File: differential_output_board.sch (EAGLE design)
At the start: 18 parts, among them IC1 ATA6563

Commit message: fixed CAN termination for cat6 wiring
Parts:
- R1, R2, R3, R4: value 62R -> 49R9; MOUSER 652-CR1206FX-62R0ELF -> 71-CRCW120649R9FKEAC
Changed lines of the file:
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@@
 <part name="+3V4" library="supply1" library_urn="urn:adsk.eagle:library:371" deviceset="+3V3" device=""/>
 <part name="GND5" library="supply1" library_urn="urn:adsk.eagle:library:371" deviceset="GND" device=""/>
-<part name="R1" library="rcl" library_urn="urn:adsk.eagle:library:334" deviceset="R-EU_" device="M1206" package3d_urn="urn:adsk.eagle:package:23566/1" value="62R">
+<part name="R1" library="rcl" library_urn="urn:adsk.eagle:library:334" deviceset="R-EU_" device="M1206" package3d_urn="urn:adsk.eagle:package:23566/1" value="49R9">
 <spice>
 <pinmapping spiceprefix="R">
@@
 </pinmapping>
 </spice>
-<attribute name="MOUSER" value="652-CR1206FX-62R0ELF"/>
+<attribute name="MOUSER" value="71-CRCW120649R9FKEAC"/>
 </part>
-<part name="R2" library="rcl" library_urn="urn:adsk.eagle:library:334" deviceset="R-EU_" device="M1206" package3d_urn="urn:adsk.eagle:package:23566/1" value="62R">
+<part name="R2" library="rcl" library_urn="urn:adsk.eagle:library:334" deviceset="R-EU_" device="M1206" package3d_urn="urn:adsk.eagle:package:23566/1" value="49R9">
 <spice>
 <pinmapping spiceprefix="R">
@@
 </pinmapping>
 </spice>
-<attribute name="MOUSER" value="652-CR1206FX-62R0ELF"/>
+<attribute name="MOUSER" value="71-CRCW120649R9FKEAC"/>
 </part>
 <part name="C7" library="rcl" library_urn="urn:adsk.eagle:library:334" deviceset="C-EU" device="C0805" package3d_urn="urn:adsk.eagle:package:23617/2" value="4.7nF">
@@
 </part>
 <part name="GND6" library="supply1" library_urn="urn:adsk.eagle:library:371" deviceset="GND" device=""/>
-<part name="R3" library="rcl" library_urn="urn:adsk.eagle:library:334" deviceset="R-EU_" device="M1206" package3d_urn="urn:adsk.eagle:package:23566/1" value="62R">
+<part name="R3" library="rcl" library_urn="urn:adsk.eagle:library:334" deviceset="R-EU_" device="M1206" package3d_urn="urn:adsk.eagle:package:23566/1" value="49R9">
 <spice>
 <pinmapping spiceprefix="R">
@@
 </pinmapping>
 </spice>
-<attribute name="MOUSER" value="652-CR1206FX-62R0ELF"/>
+<attribute name="MOUSER" value="71-CRCW120649R9FKEAC"/>
 </part>
-<part name="R4" library="rcl" library_urn="urn:adsk.eagle:library:334" deviceset="R-EU_" device="M1206" package3d_urn="urn:adsk.eagle:package:23566/1" value="62R">
+<part name="R4" library="rcl" library_urn="urn:adsk.eagle:library:334" deviceset="R-EU_" device="M1206" package3d_urn="urn:adsk.eagle:package:23566/1" value="49R9">
 <spice>
 <pinmapping spiceprefix="R">
@@
 </pinmapping>
 </spice>
-<attribute name="MOUSER" value="652-CR1206FX-62R0ELF"/>
+<attribute name="MOUSER" value="71-CRCW120649R9FKEAC"/>
 </part>
 <part name="C8" library="rcl" library_urn="urn:adsk.eagle:library:334" deviceset="C-EU" device="C0805" package3d_urn="urn:adsk.eagle:package:23617/2" value="4.7nF">

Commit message: added status LEDs for power on differential output board
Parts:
- added LED1, LED2: (no value), led:LEDCHIPLED_1206
- added R5: 1k2, rcl:R-EU_M0805
- added R6: 680R, rcl:R-EU_M0805
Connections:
- new net N$13: LED1.A, R5.2
- new net N$14: LED2.A, R6.2
- net +3V3: now also R6.1
- net +5V: now also R5.1
- net GND: now also LED1.C, LED2.C
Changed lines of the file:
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@@
 <part name="SV4" library="lichtenstein_onion" deviceset="SS-51000-003" device=""/>
 <part name="SV5" library="lichtenstein_onion" deviceset="SS-51000-003" device=""/>
+<part name="LED1" library="led" library_urn="urn:adsk.eagle:library:259" deviceset="LED" device="CHIPLED_1206" package3d_urn="urn:adsk.eagle:package:15823/2">
+<attribute name="MOUSER" value="604-APTR3216SGC"/>
+</part>
+<part name="LED2" library="led" library_urn="urn:adsk.eagle:library:259" deviceset="LED" device="CHIPLED_1206" package3d_urn="urn:adsk.eagle:package:15823/2">
+<attribute name="MOUSER" value="604-APTR3216SGC"/>
+</part>
+<part name="R5" library="rcl" library_urn="urn:adsk.eagle:library:334" deviceset="R-EU_" device="M0805" package3d_urn="urn:adsk.eagle:package:23556/1" value="1k2">
+<attribute name="MOUSER" value="652-CR0805FX-1201ELF"/>
+</part>
+<part name="R6" library="rcl" library_urn="urn:adsk.eagle:library:334" deviceset="R-EU_" device="M0805" package3d_urn="urn:adsk.eagle:package:23556/1" value="680R">
+<attribute name="MOUSER" value="652-CR0805-FX6800GLF"/>
+</part>
+<part name="GND15" library="supply1" library_urn="urn:adsk.eagle:library:371" deviceset="GND" device=""/>
+<part name="P+5" library="supply1" library_urn="urn:adsk.eagle:library:371" deviceset="+5V" device=""/>
+<part name="+3V5" library="supply1" library_urn="urn:adsk.eagle:library:371" deviceset="+3V3" device=""/>
 </parts>
 <sheets>
@@
 <instance part="SV4" gate="G$1" x="40.64" y="180.34"/>
 <instance part="SV5" gate="G$1" x="40.64" y="152.4"/>
+<instance part="LED1" gate="G$1" x="35.56" y="63.5" rot="R90">
+<attribute name="MOUSER" x="35.56" y="63.5" size="1.27" layer="96" rot="R90" align="top-center" display="off"/>
+</instance>
+<instance part="LED2" gate="G$1" x="35.56" y="55.88" rot="R90">
+<attribute name="MOUSER" x="35.56" y="55.88" size="1.27" layer="96" rot="R90" align="top-center" display="off"/>
+</instance>
+<instance part="R5" gate="G$1" x="27.94" y="63.5">
+<attribute name="MOUSER" x="27.94" y="63.5" size="1.27" layer="96" align="top-center" display="off"/>
+</instance>
+<instance part="R6" gate="G$1" x="27.94" y="55.88">
+<attribute name="MOUSER" x="27.94" y="55.88" size="1.27" layer="96" align="top-center" display="off"/>
+</instance>
+<instance part="GND15" gate="1" x="43.18" y="63.5" smashed="yes" rot="R90">
+<attribute name="VALUE" x="45.72" y="63.5" size="1.778" layer="96"/>
+</instance>
+<instance part="P+5" gate="1" x="20.32" y="63.5" smashed="yes" rot="R90">
+<attribute name="VALUE" x="17.78" y="63.5" size="1.778" layer="96" rot="R180"/>
+</instance>
+<instance part="+3V5" gate="G$1" x="20.32" y="55.88" smashed="yes" rot="R90">
+<attribute name="VALUE" x="17.78" y="55.88" size="1.778" layer="96" rot="R180"/>
+</instance>
 </instances>
 <busses>
@@
 <pinref part="+3V4" gate="G$1" pin="+3V3"/>
 <junction x="187.96" y="78.74"/>
+</segment>
+<segment>
+<pinref part="R6" gate="G$1" pin="1"/>
+<pinref part="+3V5" gate="G$1" pin="+3V3"/>
+<junction x="22.86" y="55.88"/>
 </segment>
 </net>
@@
 <junction x="121.92" y="20.32"/>
 </segment>
+<segment>
+<pinref part="LED2" gate="G$1" pin="C"/>
+<pinref part="LED1" gate="G$1" pin="C"/>
+<wire x1="40.64" y1="63.5" x2="40.64" y2="55.88" width="0.1524" layer="91"/>
+<pinref part="GND15" gate="1" pin="GND"/>
+<junction x="40.64" y="63.5"/>
+</segment>
 </net>
 <net name="OUT3_N" class="0">
@@
 <junction x="198.12" y="78.74"/>
 </segment>
+<segment>
+<pinref part="R5" gate="G$1" pin="1"/>
+<pinref part="P+5" gate="1" pin="+5V"/>
+<junction x="22.86" y="63.5"/>
+</segment>
 </net>
 <net name="CAN_TX" class="0">
@@
 </segment>
 </net>
+<net name="N$13" class="0">
+<segment>
+<pinref part="LED1" gate="G$1" pin="A"/>
+<pinref part="R5" gate="G$1" pin="2"/>
+<junction x="33.02" y="63.5"/>
+</segment>
+</net>
+<net name="N$14" class="0">
+<segment>
+<pinref part="LED2" gate="G$1" pin="A"/>
+<pinref part="R6" gate="G$1" pin="2"/>
+<junction x="33.02" y="55.88"/>
+</segment>
+</net>

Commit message: routed differential output board
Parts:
- added WEED1: WEED, lichtenstein_onion:WEED
- C2: value 10µF -> 100nF; device rcl:CPOL-EUSMCB -> rcl:C-EUC0805; MOUSER 581-TAJB106K020RNJV -> 710-885012207072
- C3: value 100nF -> 47µF; device rcl:C-EUC0805 -> rcl:CPOL-EUCT6032; MOUSER 710-885012207072 -> 581-TAJD476M016RNJV
- C4: value 100nF -> 10µF; device rcl:C-EUC0805 -> rcl:CPOL-EUSMCB; MOUSER 710-885012207072 -> 581-TAJB106K020RNJV
- C5: value 100nF -> 4.7nF; MOUSER 710-885012207072 -> 710-885012207037
- C6: value 47µF -> 4.7nF; device rcl:CPOL-EUCT6032 -> rcl:C-EUC0805; MOUSER 581-TAJD476M016RNJV -> 710-885012207037
- C7, C8: value 4.7nF -> 100nF; MOUSER 710-885012207037 -> 710-885012207072
- R1: value 49R9 -> 1k2; device rcl:R-EU_M1206 -> rcl:R-EU_M0805; MOUSER 71-CRCW120649R9FKEAC -> 652-CR0805FX-1201ELF
- R2: value 49R9 -> 680R; device rcl:R-EU_M1206 -> rcl:R-EU_M0805; MOUSER 71-CRCW120649R9FKEAC -> 652-CR0805-FX6800GLF
- R5: value 1k2 -> 49R9; device rcl:R-EU_M0805 -> rcl:R-EU_M1206; MOUSER 652-CR0805FX-1201ELF -> 71-CRCW120649R9FKEAC
- R6: value 680R -> 49R9; device rcl:R-EU_M0805 -> rcl:R-EU_M1206; MOUSER 652-CR0805-FX6800GLF -> 71-CRCW120649R9FKEAC
- SV2: value (none) -> SS-51000-003; device con-lstb:MA12-2 -> lichtenstein_onion:SS-51000-003; MOUSER 517-30320-6002 -> (none)
- SV3: value SS-51000-003 -> (none); device lichtenstein_onion:SS-51000-003 -> con-lstb:MA12-2; MOUSER (none) -> 517-30320-6002
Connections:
- net +3V3: now also C2.1, C4.+, C7.1, R2.1, SV3.2; no longer C1.1, C2.+, C4.1, R6.1, SV2.2
- net +5V: now also C1.1, C3.+, C8.1, R1.1, SV3.4; no longer C3.1, C5.1, C6.+, R5.1, SV2.4
- net CANH: now also R3.2, SV1.6; no longer R1.2, SV1.5
- net CANH_1: now also SV1.8, SV2.6; no longer SV1.7, SV3.5
- net CANH_2: now also SV2.8, SV4.6; no longer SV3.7, SV4.5
- net CANH_3: now also SV4.8, SV5.6; no longer SV4.7, SV5.5
- net CANH_4: now also R5.1, SV5.8; no longer R4.1, SV5.7
- net CANL: now also R4.1, SV1.5; no longer R2.1, SV1.6
- net CANL_1: now also SV1.7, SV2.5; no longer SV1.8, SV3.6
- net CANL_2: now also SV2.7, SV4.5; no longer SV3.8, SV4.6
- net CANL_3: now also SV4.7, SV5.5; no longer SV4.8, SV5.6
- net CANL_4: now also R6.2, SV5.7; no longer R3.2, SV5.8
- net CAN_RX: now also SV3.23; no longer SV2.23
- net CAN_TX: now also SV3.24; no longer SV2.24
- net GND: now also C2.2, C3.-, C4.-, C6.2, SV3.1, SV3.21, SV3.22, SV3.3; no longer C2.-, C3.2, C4.2, C6.-, SV2.1, SV2.21, SV2.22, SV2.3
- net N$1: now also C5.1, R3.1, R4.2; no longer C7.1, R1.1, R2.2
- net N$13: now also R1.2; no longer R5.2
- net N$14: now also R2.2; no longer R6.2
- net N$2: now also C6.1, R5.2, R6.1; no longer C8.1, R3.1, R4.2
- net OUT0_N: now also SV1.1, SV3.20; no longer SV1.2, SV2.8
- net OUT0_P: now also SV1.2, SV3.18; no longer SV1.1, SV2.6
- net OUT1_N: now also SV1.3, SV3.16; no longer SV1.4, SV2.12
- net OUT1_P: now also SV1.4, SV3.14; no longer SV1.3, SV2.10
- net OUT2_N: now also SV2.1, SV3.12; no longer SV2.16, SV3.2
- net OUT2_P: now also SV2.2, SV3.10; no longer SV2.14, SV3.1
- net OUT3_N: now also SV2.3, SV3.8; no longer SV2.20, SV3.4, SV4.2
- net OUT3_P: now also SV2.4, SV3.6; no longer SV2.18, SV3.3, SV4.1
- net OUT4_N: now also SV3.7, SV4.3; no longer SV2.7, SV4.4
- net OUT4_P: now also SV3.5, SV4.4; no longer SV2.5, SV4.3
- net OUT5_N: now also SV3.11, SV4.1; no longer SV2.11, SV5.2
- net OUT5_P: now also SV3.9, SV4.2; no longer SV2.9, SV5.1
- net OUT6_N: now also SV3.15, SV5.3; no longer SV2.15, SV5.4
- net OUT6_P: now also SV3.13, SV5.4; no longer SV2.13, SV5.3
- net OUT7_N: now also SV3.19, SV5.1; no longer SV2.19
- net OUT7_P: now also SV3.17, SV5.2; no longer SV2.17
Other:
- moved on the sheet: C1, C5, C7, C8, R1, R2, R3, R4, R5, R6

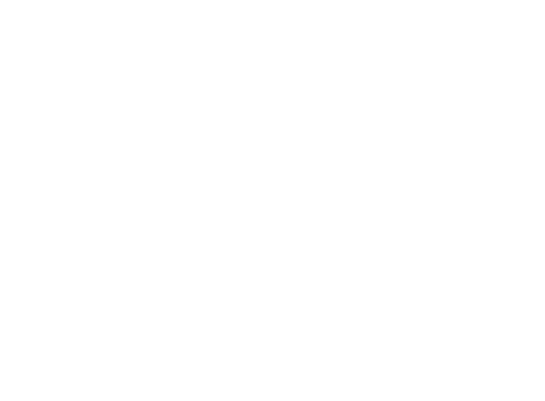
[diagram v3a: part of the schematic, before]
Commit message: added holes to differential output board
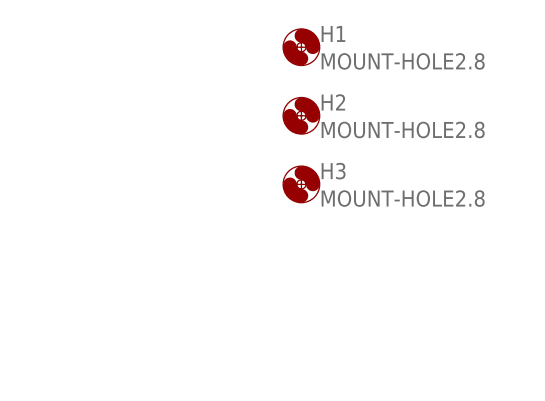
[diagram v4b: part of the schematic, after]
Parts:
- added H1, H2, H3: MOUNT-HOLE2.8, holes:MOUNT-HOLE2.8
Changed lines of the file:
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@@
 <part name="+3V32" library="supply1" library_urn="urn:adsk.eagle:library:371" deviceset="+3V3" device=""/>
 <part name="WEED1" library="lichtenstein_onion" deviceset="WEED" device=""/>
+<part name="H1" library="holes" library_urn="urn:adsk.eagle:library:237" deviceset="MOUNT-HOLE" device="2.8" package3d_urn="urn:adsk.eagle:package:14271/1"/>
+<part name="H2" library="holes" library_urn="urn:adsk.eagle:library:237" deviceset="MOUNT-HOLE" device="2.8" package3d_urn="urn:adsk.eagle:package:14271/1"/>
+<part name="H3" library="holes" library_urn="urn:adsk.eagle:library:237" deviceset="MOUNT-HOLE" device="2.8" package3d_urn="urn:adsk.eagle:package:14271/1"/>
 </parts>
 <sheets>
@@
 </instance>
 <instance part="WEED1" gate="G$1" x="147.32" y="38.1"/>
+<instance part="H1" gate="G$1" x="223.52" y="180.34"/>
+<instance part="H2" gate="G$1" x="223.52" y="172.72"/>
+<instance part="H3" gate="G$1" x="223.52" y="165.1"/>
 </instances>
 <busses>

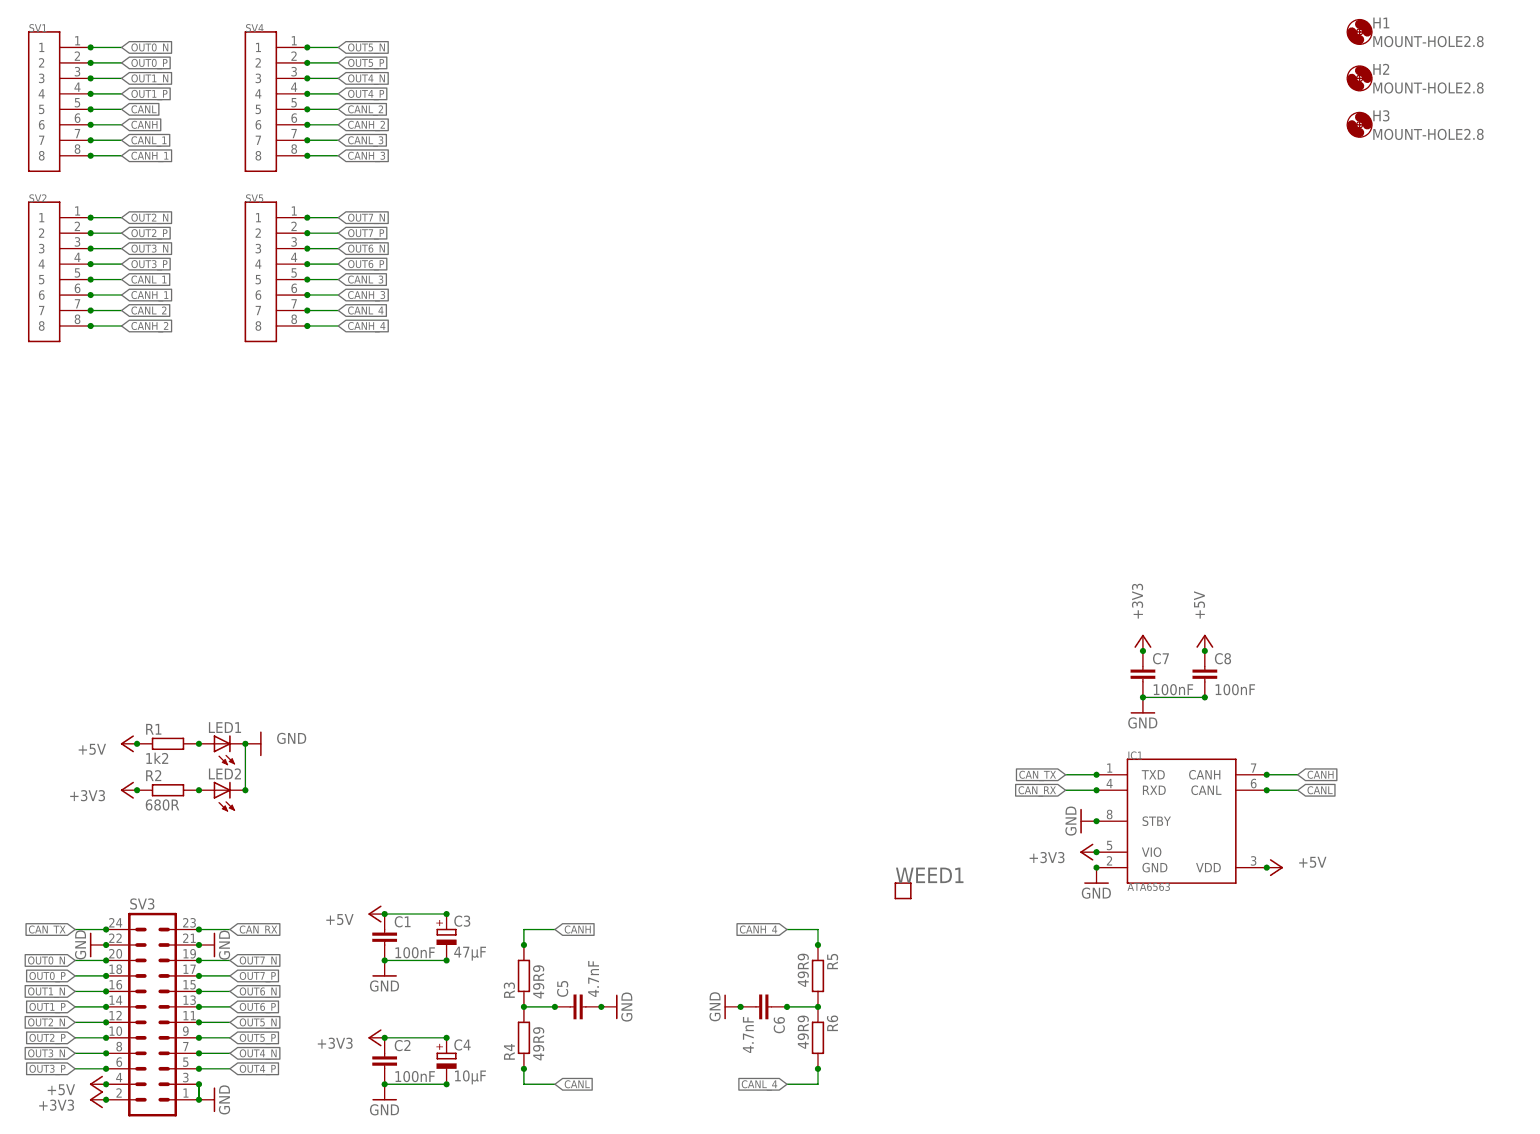
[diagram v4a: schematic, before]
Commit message: More tweaks to the differential output board
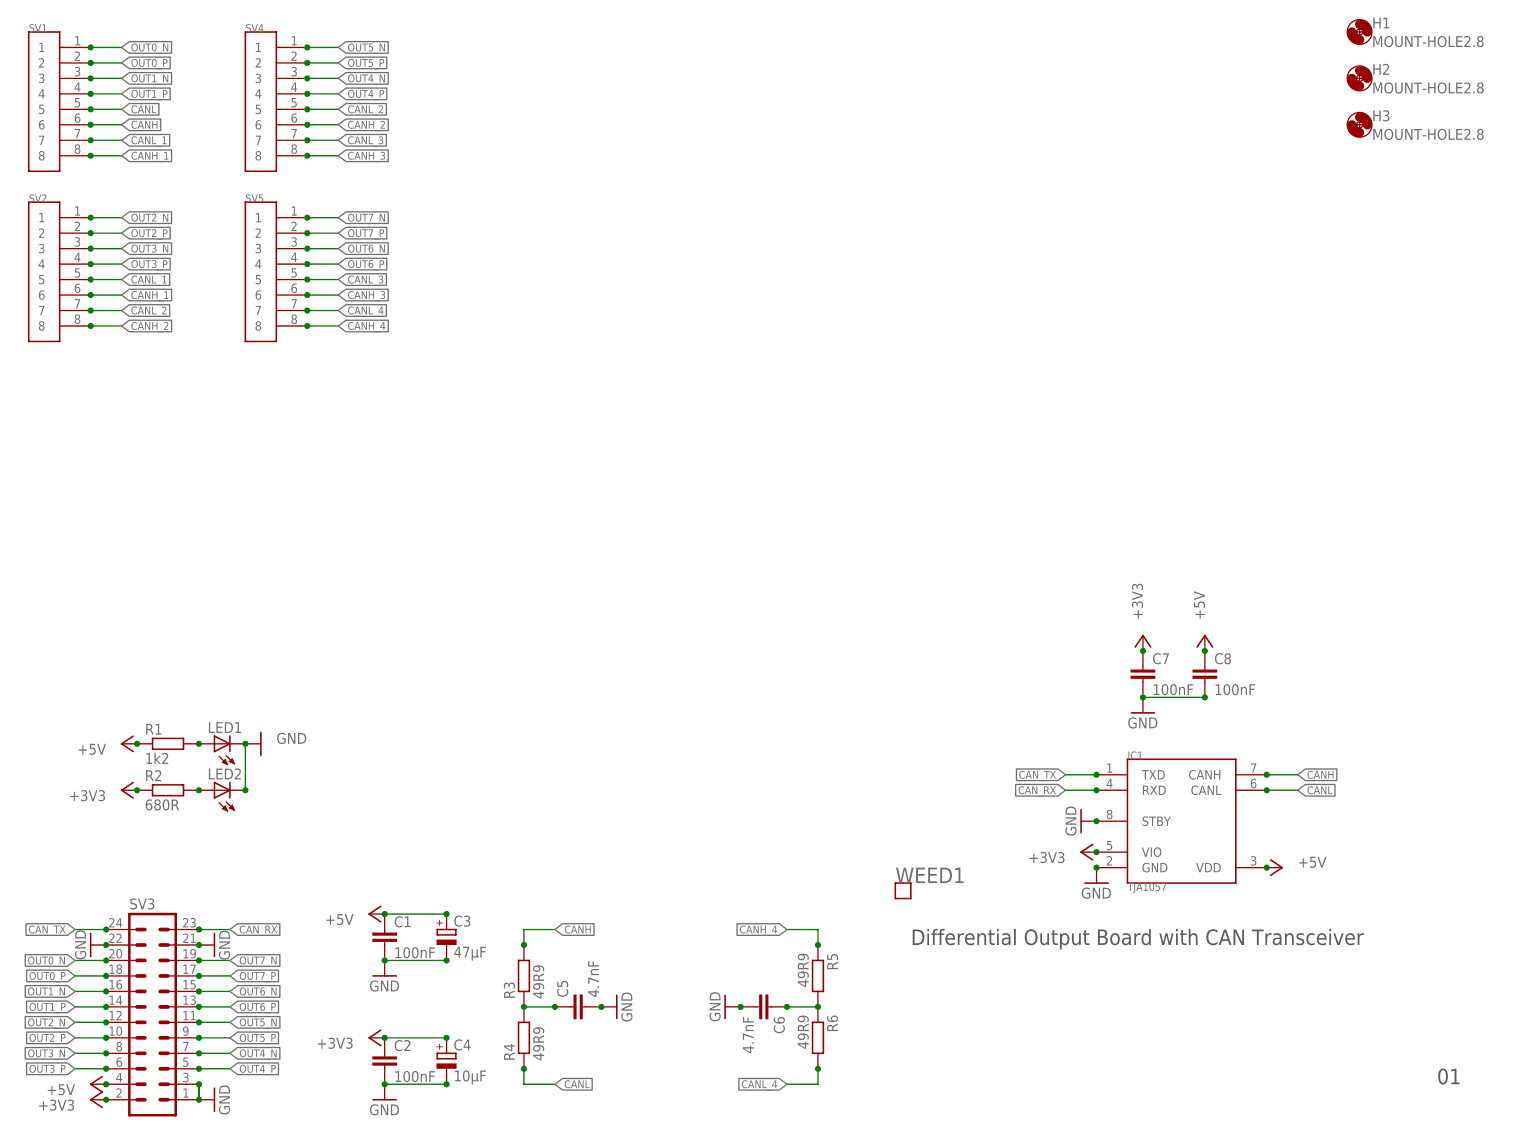
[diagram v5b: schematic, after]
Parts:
- IC1: value ATA6563 -> TJA1057; device lichtenstein_onion:ATA6563 -> lichtenstein_onion:TJA1057
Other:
- note added: "01"
- note added: "Differential Output Board with CAN Transceiver"
